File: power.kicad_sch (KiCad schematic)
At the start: 32 parts, among them IC301 XL1509-5.0E1, IC302 SY8113BADC, SW301 1FS1T1B9M2RES-5, X301 KF2EDGR-3.81-3P

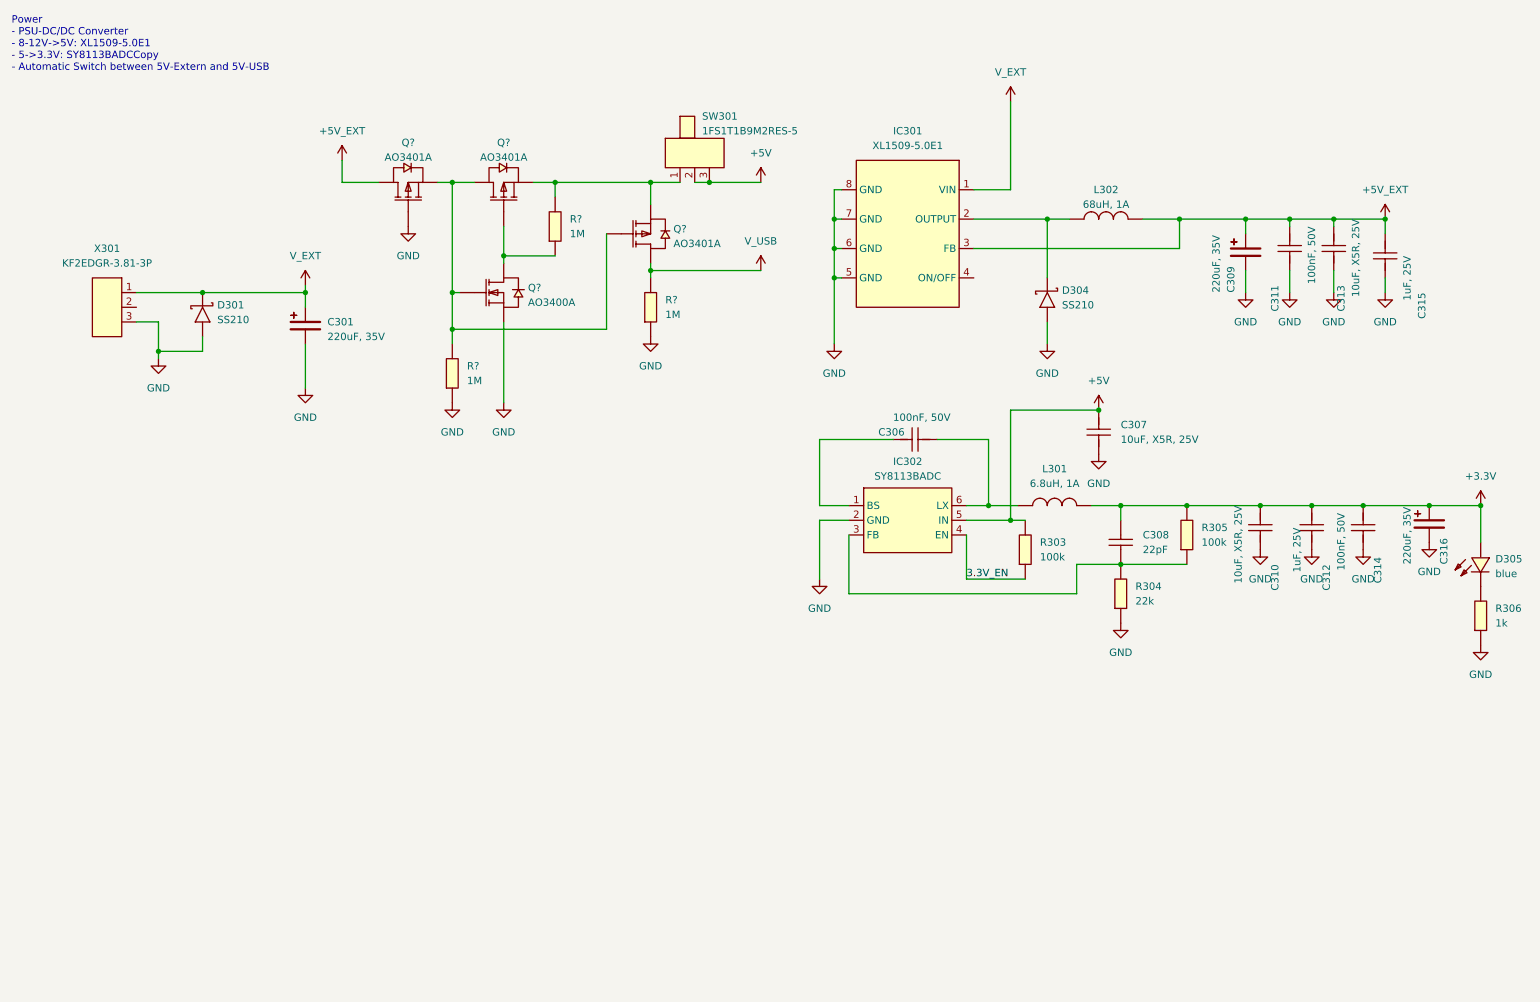
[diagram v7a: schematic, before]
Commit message: reassign symbol references after page movements. Place in pcb
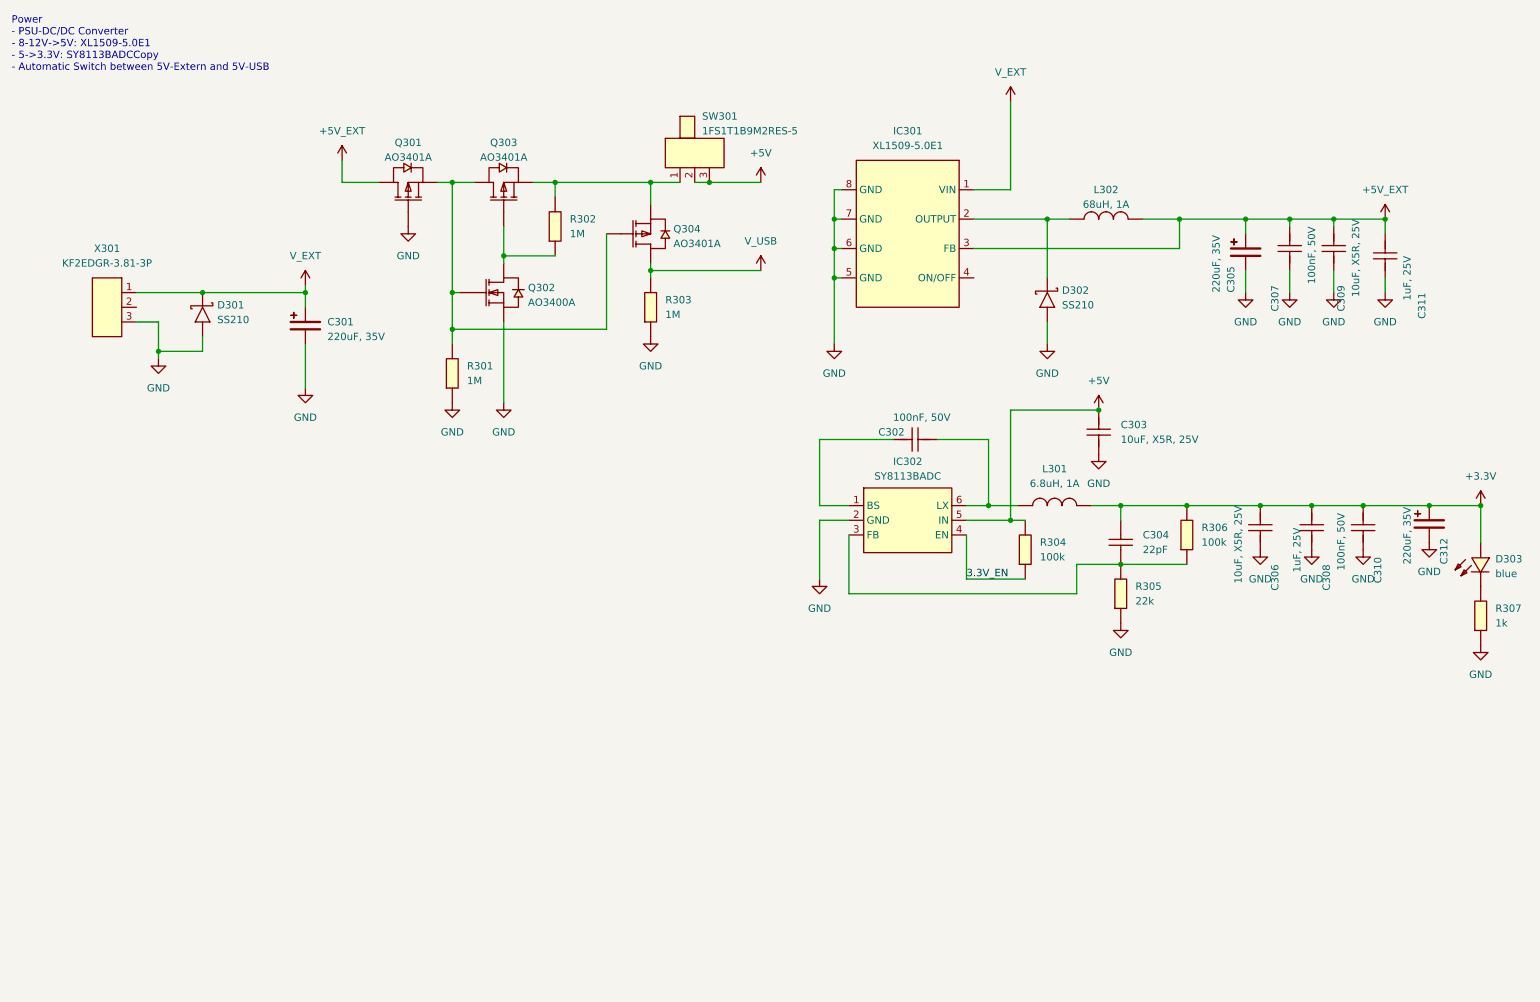
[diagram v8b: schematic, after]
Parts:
- C301: footprint CAP-SMD_BD8.0-L8.3-W8.3-RD -> eduboardv2:CAP-SMD_BD8.0-L8.3-W8.3-RD
- C302: renamed from C306; footprint C0402 -> eduboardv2:C0402
- C303: renamed from C307; footprint C0603 -> eduboardv2:C0603
- C304: renamed from C308; footprint C0402 -> eduboardv2:C0402
- C305: renamed from C309; footprint CAP-SMD_BD8.0-L8.3-W8.3-RD -> eduboardv2:CAP-SMD_BD8.0-L8.3-W8.3-RD
- C306: renamed from C310; footprint C0603 -> eduboardv2:C0603
- C307: renamed from C311; footprint C0402 -> eduboardv2:C0402
- C308: renamed from C312; footprint C0402 -> eduboardv2:C0402
- C309: renamed from C313; footprint C0603 -> eduboardv2:C0603
- C310: renamed from C314; footprint C0402 -> eduboardv2:C0402
- C311: renamed from C315; footprint C0402 -> eduboardv2:C0402
- C312: renamed from C316; footprint CAP-SMD_BD8.0-L8.3-W8.3-RD -> eduboardv2:CAP-SMD_BD8.0-L8.3-W8.3-RD
- D301: footprint SMA_L4.3-W2.6-LS5.2-RD -> eduboardv2:SMA_L4.3-W2.6-LS5.2-RD
- D302: renamed from D304; footprint SMA_L4.3-W2.6-LS5.2-RD -> eduboardv2:SMA_L4.3-W2.6-LS5.2-RD
- D303: renamed from D305; footprint LED0603-R-RD_BLUE -> eduboardv2:LED0603-R-RD_BLUE
- IC301: footprint SOIC-8_L5.0-W4.0-P1.27-LS6.0-BL -> eduboardv2:SOIC-8_L5.0-W4.0-P1.27-LS6.0-BL
- IC302: footprint TSOT-23-6_L2.9-W1.6-P0.95-LS2.8-BR -> eduboardv2:TSOT-23-6_L2.9-W1.6-P0.95-LS2.8-BR
- L301: footprint IND-SMD_L4.0-W4.0 -> eduboardv2:IND-SMD_L4.0-W4.0
- L302: footprint IND-SMD_L6.0-W6.0_FNR60XXS -> eduboardv2:IND-SMD_L6.0-W6.0_FNR60XXS
- Q301, Q303, Q304: renamed from Q?; footprint SOT-23_L2.9-W1.3-P1.90-LS2.4-BR -> eduboardv2:SOT-23_L2.9-W1.3-P1.90-LS2.4-BR
- Q302: renamed from Q?; footprint SOT-23-3_L2.9-W1.6-P1.90-LS2.8-BR -> eduboardv2:SOT-23-3_L2.9-W1.6-P1.90-LS2.8-BR
- R301, R302, R303: renamed from R?; footprint R0402 -> eduboardv2:R0402
- R304: renamed from R303; footprint R0402 -> eduboardv2:R0402
- R305: renamed from R304; footprint R0402 -> eduboardv2:R0402
- R306: renamed from R305; footprint R0402 -> eduboardv2:R0402
- R307: renamed from R306; footprint R0402 -> eduboardv2:R0402
- SW301: footprint SW-TH_1FS1T1B9M2RES-5 -> eduboardv2:SW-TH_1FS1T1B9M2RES-5
- X301: footprint CONN-TH_3P-P3.81_KF2EDGR-3.81-3P -> eduboardv2:CONN-TH_3P-P3.81_KF2EDGR-3.81-3P
